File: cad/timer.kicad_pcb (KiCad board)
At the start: 2 copper layers, 47 x 47 mm, 30 parts, among them Q1 BS170, Q2 BS170, U1 ATMEGA328P-PU, Y1 32.768kHz

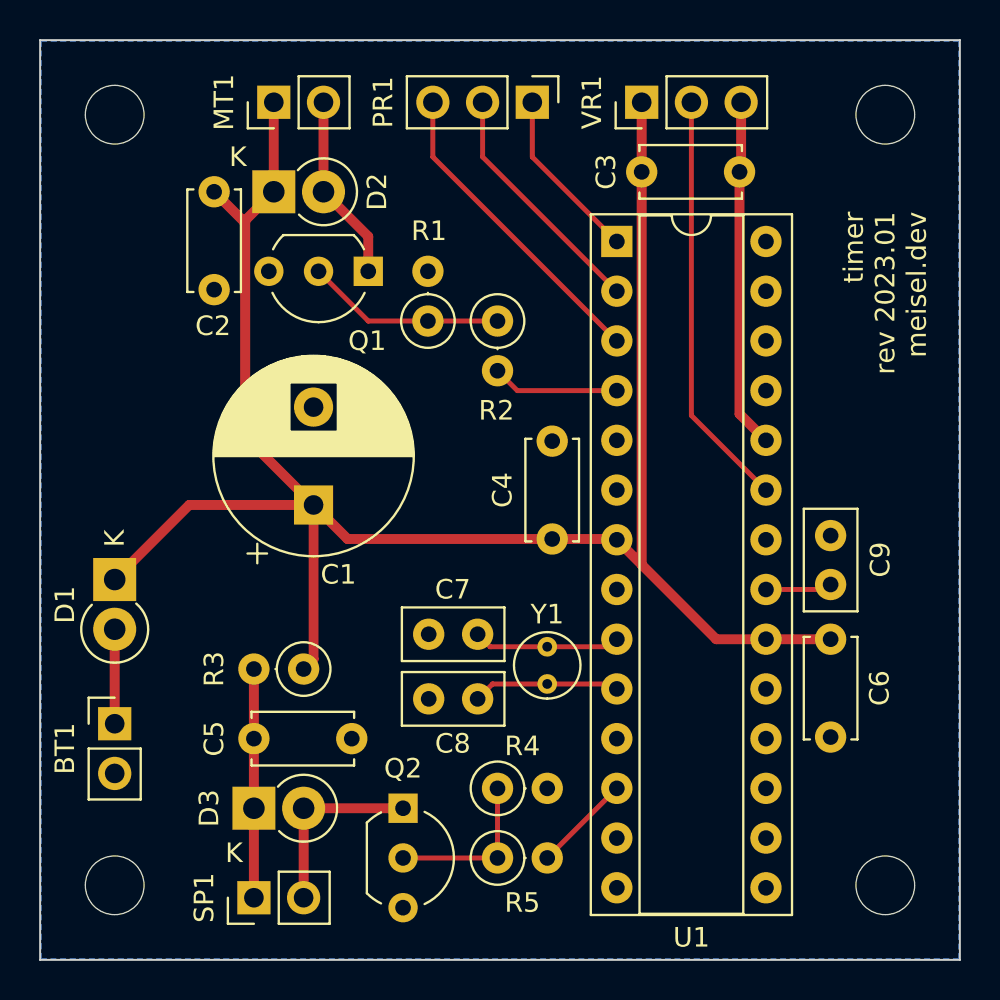
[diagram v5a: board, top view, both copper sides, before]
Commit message: Add markers for positive terminals
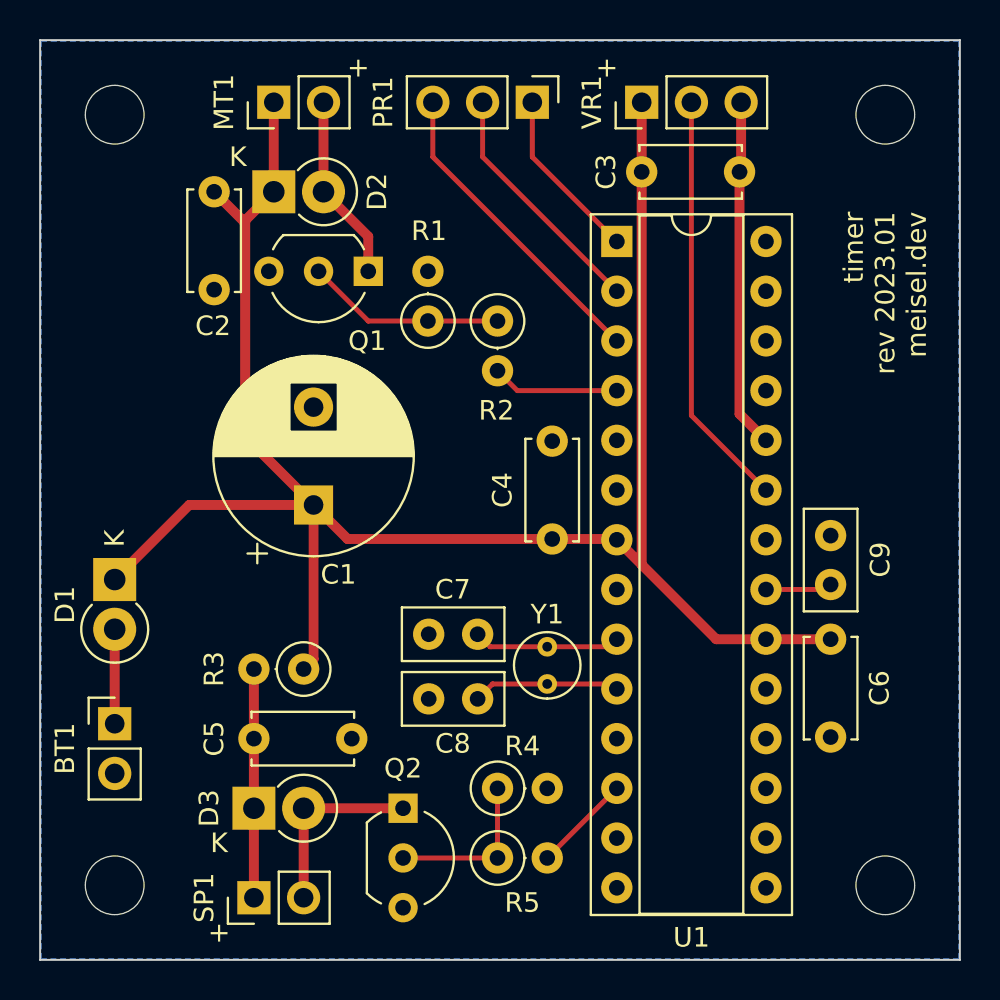
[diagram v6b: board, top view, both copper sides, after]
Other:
- board text added: "+"
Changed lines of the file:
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@@
       (effects (font (size 1 1) (thickness 0.15)))
     )
-    (fp_text user "K" (at -1.016 2.286) (layer "F.SilkS")
+    (fp_text user "K" (at -1.778 1.778) (layer "F.SilkS")
       (effects (font (size 1 1) (thickness 0.15)))
     )
@@
   )
   (gr_rect (start 121.92 69.215) (end 168.91 116.205) (layer "Edge.Cuts") (width 0.1) (fill none))
+  (gr_text "+" (at 150.876 70.612) (layer "F.SilkS")
+    (effects (font (size 1 1) (thickness 0.15)))
+  )
+  (gr_text "+" (at 131.064 114.808) (layer "F.SilkS")
+    (effects (font (size 1 1) (thickness 0.15)))
+  )
+  (gr_text "+" (at 138.176 70.612) (layer "F.SilkS")
+    (effects (font (size 1 1) (thickness 0.15)))
+  )
   (gr_text "timer\nrev 2023.01\nmeisel.dev" (at 165.1 77.978 90) (layer "F.SilkS")
     (effects (font (size 0.999998 0.999998) (thickness 0.2)) (justify right))

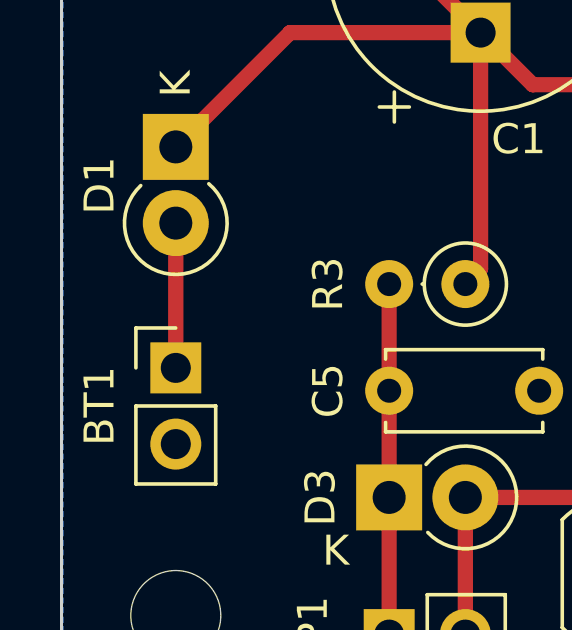
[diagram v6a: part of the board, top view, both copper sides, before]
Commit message: Missed one positive terminal marker
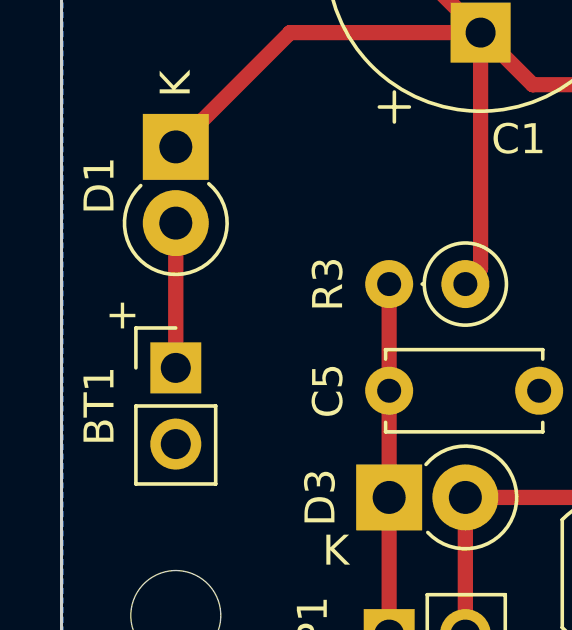
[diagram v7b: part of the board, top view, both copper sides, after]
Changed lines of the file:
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@@
   (net 11 "Net-(U1-Pad23)")
   (net 12 "Net-(D3-Pad2)")
-  (net 13 "Net-(U1-Pad4)")
+  (net 13 "Net-(R2-Pad2)")
   (net 14 "unconnected-(U1-Pad18)")
   (net 15 "unconnected-(U1-Pad6)")
@@
       (net 9 "Net-(PR1-Pad3)") (pinfunction "(PCINT17/TXD)PD1") (pintype "bidirectional"))
     (pad "4" thru_hole oval (at 0 7.62) (size 1.6 1.6) (drill 0.8) (layers *.Cu *.Mask)
-      (net 13 "Net-(U1-Pad4)") (pinfunction "(PCINT18/INT0)PD2") (pintype "bidirectional"))
+      (net 13 "Net-(R2-Pad2)") (pinfunction "(PCINT18/INT0)PD2") (pintype "bidirectional"))
     (pad "5" thru_hole oval (at 0 10.16) (size 1.6 1.6) (drill 0.8) (layers *.Cu *.Mask)
       (net 27 "unconnected-(U1-Pad5)") (pinfunction "(PCINT19/OC2B/INT1)PD3") (pintype "bidirectional+no_connect"))
@@
       (net 10 "Net-(Q1-Pad2)") (pintype "passive"))
     (pad "2" thru_hole oval (at 2.54 0 270) (size 1.6 1.6) (drill 0.8) (layers *.Cu *.Mask)
-      (net 13 "Net-(U1-Pad4)") (pintype "passive"))
+      (net 13 "Net-(R2-Pad2)") (pintype "passive"))
     (model "${KICAD6_3DMODEL_DIR}/Resistor_THT.3dshapes/R_Axial_DIN0207_L6.3mm_D2.5mm_P2.54mm_Vertical.wrl"
       (offset (xyz 0 0 0))
@@
     (effects (font (size 0.999998 0.999998) (thickness 0.2)) (justify right))
   )
+  (gr_text "+" (at 123.952 102.362) (layer "F.SilkS")
+    (effects (font (size 1 1) (thickness 0.15)))
+  )
   (dimension (type aligned) (layer "Dwgs.User")
